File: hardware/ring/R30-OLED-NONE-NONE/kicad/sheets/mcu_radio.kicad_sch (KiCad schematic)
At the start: 0 parts

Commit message: feat(hardware): wire 30deg optical ring power and hub USB interfaces for accessibility pointing, ~$9 ring / ~$5-6 hub BOM
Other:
- note added: "MCU-side power interface scaffold: these labels match the top-sheet power contract and the firmware-facing sense/control nets."
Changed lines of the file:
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@@
   (generator_version "0.1")
   (paper "A4")
+  (text "MCU-side power interface scaffold: these labels match the top-sheet power contract and the firmware-facing sense/control nets."
+    (at 20.32 20.32 0)
+    (effects (font (size 1.27 1.27)))
+  )
+  (hierarchical_label "VREG_3V3"
+    (shape input)
+    (at 25.4 38.1 0)
+    (effects (font (size 1.27 1.27)))
+  )
+  (hierarchical_label "VBAT_SENSE"
+    (shape input)
+    (at 25.4 45.72 0)
+    (effects (font (size 1.27 1.27)))
+  )
+  (hierarchical_label "NTC_SENSE"
+    (shape input)
+    (at 25.4 53.34 0)
+    (effects (font (size 1.27 1.27)))
+  )
+  (hierarchical_label "CHARGE_EN"
+    (shape output)
+    (at 187.96 53.34 180)
+    (effects (font (size 1.27 1.27)))
+  )
   (sheet_instances
     (path "/" (page "1"))

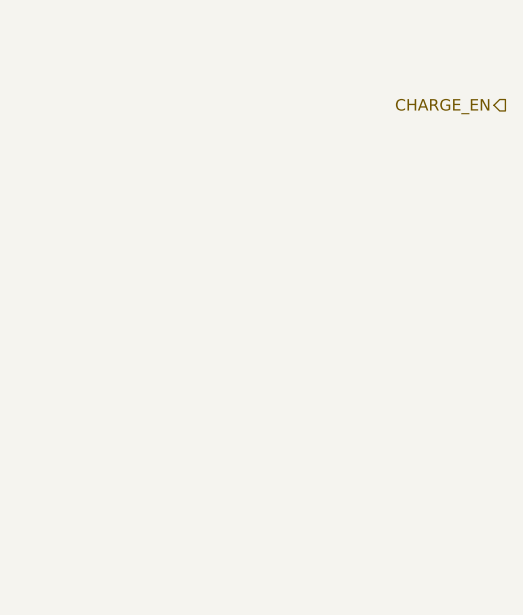
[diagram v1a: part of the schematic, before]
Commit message: feat(hardware): wire 30deg optical ring sensor/click and usb interfaces into top sheet for accessibility pointing, ~$9 ring BOM
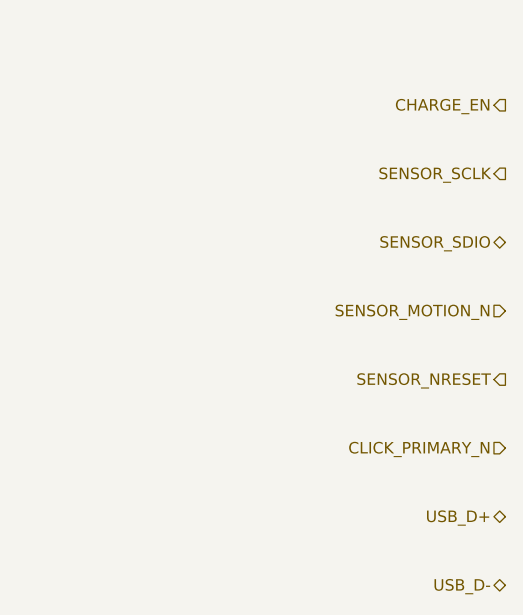
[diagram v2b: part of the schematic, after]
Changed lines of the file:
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@@
+    (effects (font (size 1.27 1.27)))
+  )
+  (hierarchical_label "SENSOR_SCLK"
+    (shape output)
+    (at 187.96 60.96 180)
+    (effects (font (size 1.27 1.27)))
+  )
+  (hierarchical_label "SENSOR_SDIO"
+    (shape bidirectional)
+    (at 187.96 68.58 180)
+    (effects (font (size 1.27 1.27)))
+  )
+  (hierarchical_label "SENSOR_MOTION_N"
+    (shape input)
+    (at 187.96 76.2 180)
+    (effects (font (size 1.27 1.27)))
+  )
+  (hierarchical_label "SENSOR_NRESET"
+    (shape output)
+    (at 187.96 83.82 180)
+    (effects (font (size 1.27 1.27)))
+  )
+  (hierarchical_label "CLICK_PRIMARY_N"
+    (shape input)
+    (at 187.96 91.44 180)
+    (effects (font (size 1.27 1.27)))
+  )
+  (hierarchical_label "USB_D+"
+    (shape bidirectional)
+    (at 187.96 99.06 180)
+    (effects (font (size 1.27 1.27)))
+  )
+  (hierarchical_label "USB_D-"
+    (shape bidirectional)
+    (at 187.96 106.68 180)
     (effects (font (size 1.27 1.27)))
   )

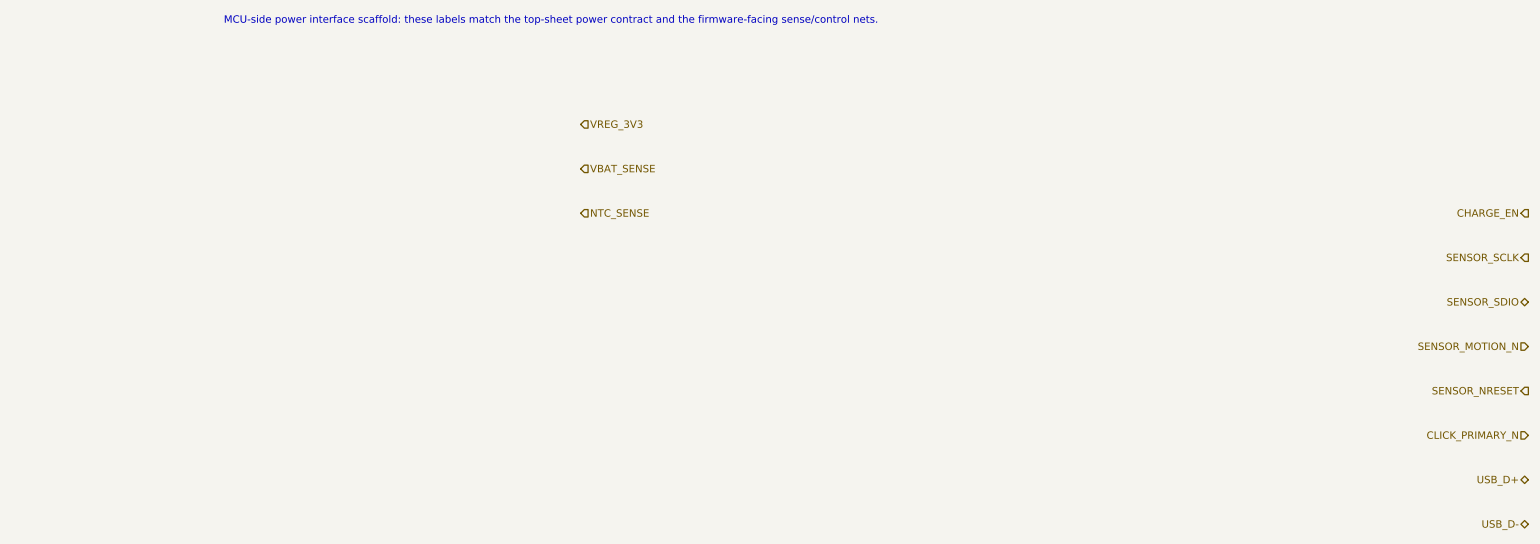
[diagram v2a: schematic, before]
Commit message: feat(hardware): lock R30 sense and schematic baseline
Design disclosure: sensing mechanism PAW3204-class optical tracking; form factor R30-OLED-NONE-NONE fingertip ring, active 30-degree ring packet; intended use BLE HID pointing for accessibility; BOM estimate ~$5.30-9.45.

Record the accepted 2N7002 charge-gate path, R7-R11 sense/status values, current KiCad red baseline, and directly linked packet truth docs.
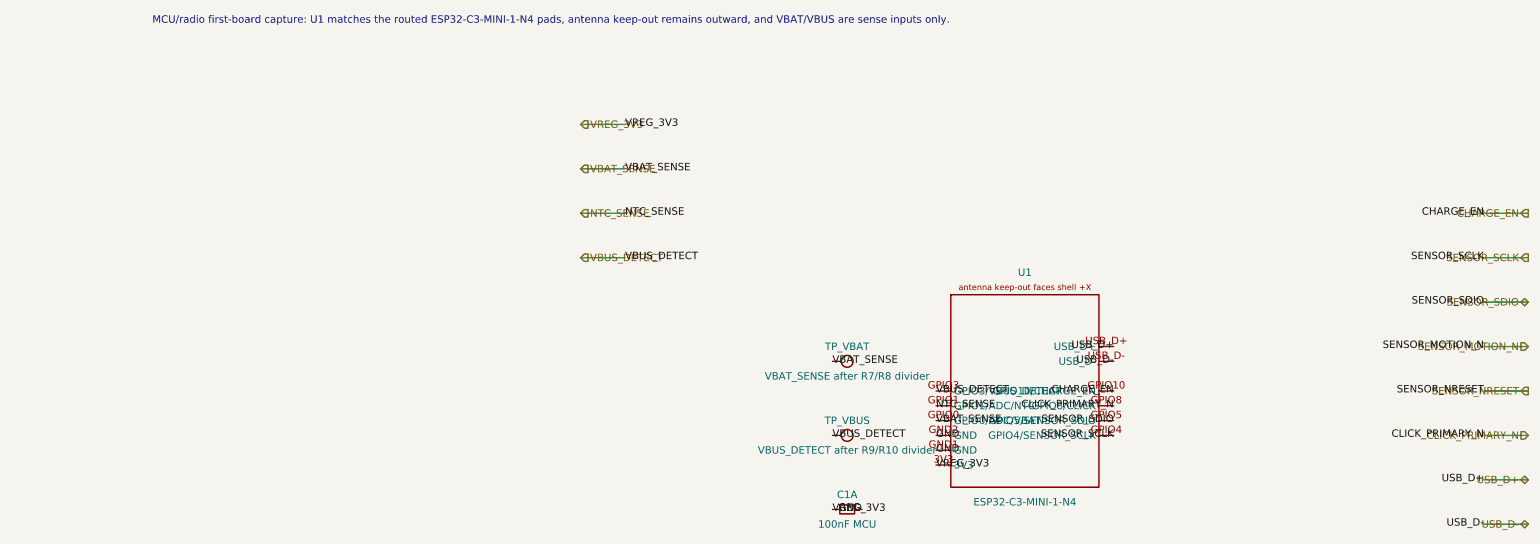
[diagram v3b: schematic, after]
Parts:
- added C1A: 100nF MCU, Capacitor_SMD:C_0402_1005Metric, symbol PowerFinger:C_0402_SUPPORT
- added TP_VBAT: VBAT_SENSE after R7/R8 divider, TestPoint:TestPoint_Pad_D1.0mm, symbol PowerFinger:TESTPAD_1MM
- added TP_VBUS: VBUS_DETECT after R9/R10 divider, TestPoint:TestPoint_Pad_D1.0mm, symbol PowerFinger:TESTPAD_1MM
- added U1: ESP32-C3-MINI-1-N4, PowerFinger_Ring:ESP32-C3-MINI-1_N4_Module_P0_AntennaRight, symbol PowerFinger:ESP32-C3-MINI-1-N4_FirstBoard
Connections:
- net CHARGE_EN: now also U1.GPIO10 (GPIO10/CHARGE_EN)
- net CLICK_PRIMARY_N: now also U1.GPIO8 (GPIO8/CLICK)
- net NTC_SENSE: now also U1.GPIO1 (GPIO1/ADC/NTC)
- net SENSOR_SCLK: now also U1.GPIO4 (GPIO4/SENSOR_SCLK)
- net SENSOR_SDIO: now also U1.GPIO5 (GPIO5/SENSOR_SDIO)
- net USB_D+: now also U1.USB_D+
- net USB_D-: now also U1.USB_D-
- net VBAT_SENSE: now also TP_VBAT.1 (TP), U1.GPIO0 (GPIO0/ADC/VBAT)
- net VREG_3V3: now also C1A.1, U1.3V3
- new net GND: C1A.2, U1.GND1 (GND), U1.GND2 (GND)
- new net VBUS_DETECT: TP_VBUS.1 (TP), U1.GPIO3 (GPIO3/VBUS_DETECT)
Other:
- note added: "MCU/radio first-board capture: U1 matches the routed ESP32-C3-MINI-1-N4 pads, antenna keep-out remains outward, and VBAT/VBUS are sense inputs only."
- note removed: "MCU-side power interface scaffold: these labels match the top-sheet power contract and the firmware-facing sense/control nets."
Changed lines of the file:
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@@
   (generator_version "0.1")
   (paper "A4")
-  (text "MCU-side power interface scaffold: these labels match the top-sheet power contract and the firmware-facing sense/control nets."
+  (text "MCU/radio first-board capture: U1 matches the routed ESP32-C3-MINI-1-N4 pads, antenna keep-out remains outward, and VBAT/VBUS are sense inputs only."
     (at 20.32 20.32 0)
     (effects (font (size 1.27 1.27)))
   )
-  (hierarchical_label "VREG_3V3"
-    (shape input)
-    (at 25.4 38.1 0)
+  (hierarchical_label "VREG_3V3" (shape input) (at 25.4 38.1 0)
     (effects (font (size 1.27 1.27)))
   )
-  (hierarchical_label "VBAT_SENSE"
-    (shape input)
-    (at 25.4 45.72 0)
+  (hierarchical_label "VBAT_SENSE" (shape input) (at 25.4 45.72 0)
     (effects (font (size 1.27 1.27)))
   )
-  (hierarchical_label "NTC_SENSE"
-    (shape input)
-    (at 25.4 53.34 0)
+  (hierarchical_label "NTC_SENSE" (shape input) (at 25.4 53.34 0)
     (effects (font (size 1.27 1.27)))
   )
-  (hierarchical_label "CHARGE_EN"
-    (shape output)
-    (at 187.96 53.34 180)
+  (hierarchical_label "VBUS_DETECT" (shape input) (at 25.4 60.96 0)
     (effects (font (size 1.27 1.27)))
   )
-  (hierarchical_label "SENSOR_SCLK"
-    (shape output)
-    (at 187.96 60.96 180)
+  (hierarchical_label "CHARGE_EN" (shape output) (at 187.96 53.34 180)
     (effects (font (size 1.27 1.27)))
   )
-  (hierarchical_label "SENSOR_SDIO"
-    (shape bidirectional)
-    (at 187.96 68.58 180)
+  (hierarchical_label "SENSOR_SCLK" (shape output) (at 187.96 60.96 180)
     (effects (font (size 1.27 1.27)))
   )
-  (hierarchical_label "SENSOR_MOTION_N"
-    (shape input)
-    (at 187.96 76.2 180)
+  (hierarchical_label "SENSOR_SDIO" (shape bidirectional) (at 187.96 68.58 180)
     (effects (font (size 1.27 1.27)))
   )
-  (hierarchical_label "SENSOR_NRESET"
-    (shape output)
-    (at 187.96 83.82 180)
+  (hierarchical_label "SENSOR_MOTION_N" (shape input) (at 187.96 76.2 180)
     (effects (font (size 1.27 1.27)))
   )
-  (hierarchical_label "CLICK_PRIMARY_N"
-    (shape input)
-    (at 187.96 91.44 180)
+  (hierarchical_label "SENSOR_NRESET" (shape output) (at 187.96 83.82 180)
     (effects (font (size 1.27 1.27)))
   )
-  (hierarchical_label "USB_D+"
-    (shape bidirectional)
-    (at 187.96 99.06 180)
+  (hierarchical_label "CLICK_PRIMARY_N" (shape input) (at 187.96 91.44 180)
     (effects (font (size 1.27 1.27)))
   )
-  (hierarchical_label "USB_D-"
-    (shape bidirectional)
-    (at 187.96 106.68 180)
+  (hierarchical_label "USB_D+" (shape bidirectional) (at 187.96 99.06 180)
     (effects (font (size 1.27 1.27)))
   )
+  (hierarchical_label "USB_D-" (shape bidirectional) (at 187.96 106.68 180)
+    (effects (font (size 1.27 1.27)))
+  )
+  (wire (pts (xy 25.4 38.1) (xy 33.02 38.1)) (stroke (width 0) (type default) (color 0 0 0 0)))
+  (wire (pts (xy 25.4 45.72) (xy 33.02 45.72)) (stroke (width 0) (type default) (color 0 0 0 0)))
+  (wire (pts (xy 25.4 53.34) (xy 33.02 53.34)) (stroke (width 0) (type default) (color 0 0 0 0)))
+  (wire (pts (xy 25.4 60.96) (xy 33.02 60.96)) (stroke (width 0) (type default) (color 0 0 0 0)))
+  (wire (pts (xy 180.34 53.34) (xy 187.96 53.34)) (stroke (width 0) (type default) (color 0 0 0 0)))
+  (wire (pts (xy 180.34 60.96) (xy 187.96 60.96)) (stroke (width 0) (type default) (color 0 0 0 0)))
+  (wire (pts (xy 180.34 68.58) (xy 187.96 68.58)) (stroke (width 0) (type default) (color 0 0 0 0)))
+  (wire (pts (xy 180.34 76.2) (xy 187.96 76.2)) (stroke (width 0) (type default) (color 0 0 0 0)))
+  (wire (pts (xy 180.34 83.82) (xy 187.96 83.82)) (stroke (width 0) (type default) (color 0 0 0 0)))
+  (wire (pts (xy 180.34 91.44) (xy 187.96 91.44)) (stroke (width 0) (type default) (color 0 0 0 0)))
+  (wire (pts (xy 180.34 99.06) (xy 187.96 99.06)) (stroke (width 0) (type default) (color 0 0 0 0)))
+  (wire (pts (xy 180.34 106.68) (xy 187.96 106.68)) (stroke (width 0) (type default) (color 0 0 0 0)))
+  (label "VREG_3V3" (at 33.02 38.1 0) (effects (font (size 1.27 1.27))))
+  (label "VBAT_SENSE" (at 33.02 45.72 0) (effects (font (size 1.27 1.27))))
+  (label "NTC_SENSE" (at 33.02 53.34 0) (effects (font (size 1.27 1.27))))
+  (label "VBUS_DETECT" (at 33.02 60.96 0) (effects (font (size 1.27 1.27))))
+  (label "CHARGE_EN" (at 180.34 53.34 180) (effects (font (size 1.27 1.27))))
+  (label "SENSOR_SCLK" (at 180.34 60.96 180) (effects (font (size 1.27 1.27))))
+  (label "SENSOR_SDIO" (at 180.34 68.58 180) (effects (font (size 1.27 1.27))))
+  (label "SENSOR_MOTION_N" (at 180.34 76.2 180) (effects (font (size 1.27 1.27))))
+  (label "SENSOR_NRESET" (at 180.34 83.82 180) (effects (font (size 1.27 1.27))))
+  (label "CLICK_PRIMARY_N" (at 180.34 91.44 180) (effects (font (size 1.27 1.27))))
+  (label "USB_D+" (at 180.34 99.06 180) (effects (font (size 1.27 1.27))))
+  (label "USB_D-" (at 180.34 106.68 180) (effects (font (size 1.27 1.27))))
+  (symbol (lib_id "PowerFinger:ESP32-C3-MINI-1-N4_FirstBoard") (at 101.6 83.82 0) (unit 1)
+    (in_bom yes) (on_board yes) (dnp no)
+    (property "Reference" "U1" (at 101.6 63.5 0)
+      (effects (font (size 1.27 1.27)))
+    )
+    (property "Value" "ESP32-C3-MINI-1-N4" (at 101.6 102.87 0)
+      (effects (font (size 1.27 1.27)))
+    )
+    (property "Footprint" "PowerFinger_Ring:ESP32-C3-MINI-1_N4_Module_P0_AntennaRight" (at 101.6 105.41 0)
+      (effects (font (size 1.27 1.27)) hide)
+    )
+    (property "Datasheet" "https://www.espressif.com/sites/default/files/documentation/esp32-c3-mini-1_datasheet_en.pdf" (at 101.6 107.95 0)
+      (effects (font (size 1.27 1.27)) hide)
+    )
+    (pin "3V3")
+    (pin "GND1")
+    (pin "GPIO0")
+    (pin "GPIO1")
+    (pin "GPIO3")
+    (pin "GPIO4")
+    (pin "GPIO5")
+    (pin "GPIO8")
+    (pin "GPIO10")
+    (pin "USB_D-")
+    (pin "USB_D+")
+    (pin "GND2")
+    (instances
+      (project "r30_oled_none_none"
+        (path "/" (reference "U1") (unit 1))
+      )
+    )
+  )
+  (symbol (lib_id "PowerFinger:C_0402_SUPPORT") (at 71.12 104.14 0) (unit 1)
+    (in_bom yes) (on_board yes) (dnp no)
+    (property "Reference" "C1A" (at 71.12 101.6 0)
+      (effects (font (size 1.27 1.27)))
+    )
+    (property "Value" "100nF MCU" (at 71.12 106.68 0)
+      (effects (font (size 1.27 1.27)))
+    )
+    (property "Footprint" "Capacitor_SMD:C_0402_1005Metric" (at 71.12 109.22 0)
+      (effects (font (size 1.27 1.27)) hide)
+    )
+    (property "Datasheet" "" (at 71.12 111.76 0)
+      (effects (font (size 1.27 1.27)) hide)
+    )
+    (pin "1")
+    (pin "2")
+    (instances
+      (project "r30_oled_none_none"
+        (path "/" (reference "C1A") (unit 1))
+      )
+    )
+  )
+  (symbol (lib_id "PowerFinger:TESTPAD_1MM") (at 71.12 78.74 0) (unit 1)
+    (in_bom yes) (on_board yes) (dnp no)
+    (property "Reference" "TP_VBAT" (at 71.12 76.2 0)
+      (effects (font (size 1.27 1.27)))
+    )
+    (property "Value" "VBAT_SENSE after R7/R8 divider" (at 71.12 81.28 0)
+      (effects (font (size 1.27 1.27)))
+    )
+    (property "Footprint" "TestPoint:TestPoint_Pad_D1.0mm" (at 71.12 83.82 0)
+      (effects (font (size 1.27 1.27)) hide)
+    )
+    (pin "1")
+    (instances
+      (project "r30_oled_none_none"
+        (path "/" (reference "TP_VBAT") (unit 1))
+      )
+    )
+  )
+  (symbol (lib_id "PowerFinger:TESTPAD_1MM") (at 71.12 91.44 0) (unit 1)
+    (in_bom yes) (on_board yes) (dnp no)
+    (property "Reference" "TP_VBUS" (at 71.12 88.9 0)
+      (effects (font (size 1.27 1.27)))
+    )
+    (property "Value" "VBUS_DETECT after R9/R10 divider" (at 71.12 93.98 0)
+      (effects (font (size 1.27 1.27)))
+    )
+    (property "Footprint" "TestPoint:TestPoint_Pad_D1.0mm" (at 71.12 96.52 0)
+      (effects (font (size 1.27 1.27)) hide)
+    )
+    (pin "1")
+    (instances
+      (project "r30_oled_none_none"
+        (path "/" (reference "TP_VBUS") (unit 1))
+      )
+    )
+  )
+  (label "VREG_3V3" (at 86.36 96.52 0) (effects (font (size 1.27 1.27))))
+  (label "GND" (at 86.36 93.98 0) (effects (font (size 1.27 1.27))))
+  (label "GND" (at 86.36 91.44 0) (effects (font (size 1.27 1.27))))
+  (label "VBAT_SENSE" (at 86.36 88.9 0) (effects (font (size 1.27 1.27))))
+  (label "NTC_SENSE" (at 86.36 86.36 0) (effects (font (size 1.27 1.27))))
+  (label "VBUS_DETECT" (at 86.36 83.82 0) (effects (font (size 1.27 1.27))))
+  (label "SENSOR_SCLK" (at 116.84 91.44 180) (effects (font (size 1.27 1.27))))
+  (label "SENSOR_SDIO" (at 116.84 88.9 180) (effects (font (size 1.27 1.27))))
+  (label "CLICK_PRIMARY_N" (at 116.84 86.36 180) (effects (font (size 1.27 1.27))))
+  (label "CHARGE_EN" (at 116.84 83.82 180) (effects (font (size 1.27 1.27))))
+  (label "USB_D-" (at 116.84 78.74 180) (effects (font (size 1.27 1.27))))
+  (label "USB_D+" (at 116.84 76.2 180) (effects (font (size 1.27 1.27))))
+  (label "VREG_3V3" (at 68.58 104.14 0) (effects (font (size 1.27 1.27))))
+  (label "GND" (at 73.66 104.14 180) (effects (font (size 1.27 1.27))))
+  (label "VBAT_SENSE" (at 68.58 78.74 0) (effects (font (size 1.27 1.27))))
+  (label "VBUS_DETECT" (at 68.58 91.44 0) (effects (font (size 1.27 1.27))))
   (sheet_instances
     (path "/" (page "1"))

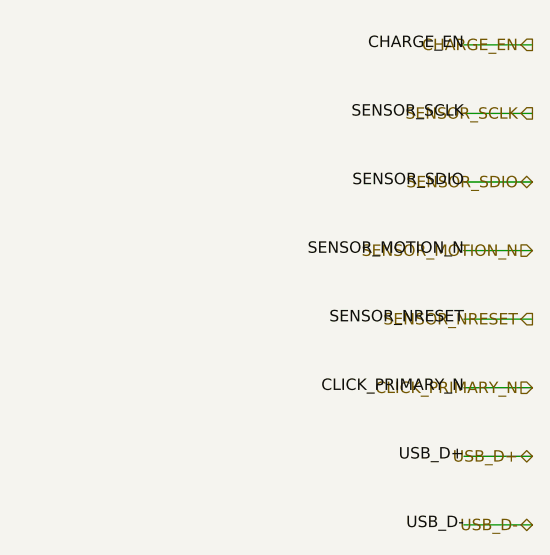
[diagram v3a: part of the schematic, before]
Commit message: fix(r30): clean schematic erc library baseline
Design disclosure: sensing mechanism PAW3204-class optical tracking; form factor R30-OLED-NONE-NONE fingertip ring, active 30-degree ring packet; intended use BLE HID pointing for accessibility; BOM estimate ~$5.30-9.45.

Materialize the project-local PowerFinger symbol and PowerFinger_Ring footprint libraries, wire sheet-interface labels, keep PAW3204 reset/motion local to sensor test pads, and update the verified KiCad snapshot to ERC=0, DRC=349, unconnected=41, parity=118.
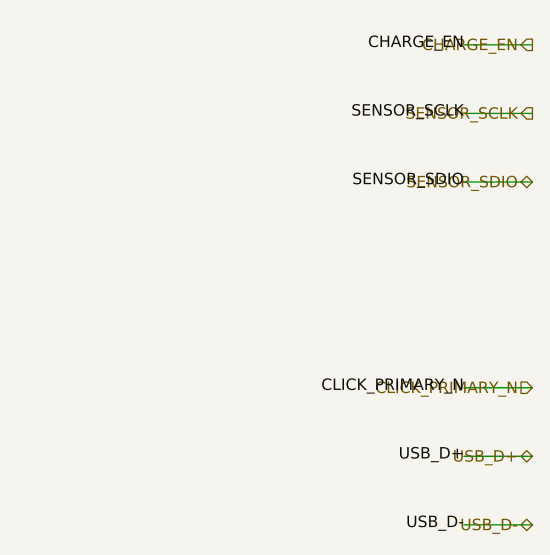
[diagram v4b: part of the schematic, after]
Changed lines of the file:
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@@
     (effects (font (size 1.27 1.27)))
   )
-  (hierarchical_label "SENSOR_MOTION_N" (shape input) (at 187.96 76.2 180)
-    (effects (font (size 1.27 1.27)))
-  )
-  (hierarchical_label "SENSOR_NRESET" (shape output) (at 187.96 83.82 180)
-    (effects (font (size 1.27 1.27)))
-  )
-  (hierarchical_label "CLICK_PRIMARY_N" (shape input) (at 187.96 91.44 180)
+      (hierarchical_label "CLICK_PRIMARY_N" (shape input) (at 187.96 91.44 180)
     (effects (font (size 1.27 1.27)))
   )
@@
   (wire (pts (xy 180.34 60.96) (xy 187.96 60.96)) (stroke (width 0) (type default) (color 0 0 0 0)))
   (wire (pts (xy 180.34 68.58) (xy 187.96 68.58)) (stroke (width 0) (type default) (color 0 0 0 0)))
-  (wire (pts (xy 180.34 76.2) (xy 187.96 76.2)) (stroke (width 0) (type default) (color 0 0 0 0)))
-  (wire (pts (xy 180.34 83.82) (xy 187.96 83.82)) (stroke (width 0) (type default) (color 0 0 0 0)))
-  (wire (pts (xy 180.34 91.44) (xy 187.96 91.44)) (stroke (width 0) (type default) (color 0 0 0 0)))
+      (wire (pts (xy 180.34 91.44) (xy 187.96 91.44)) (stroke (width 0) (type default) (color 0 0 0 0)))
   (wire (pts (xy 180.34 99.06) (xy 187.96 99.06)) (stroke (width 0) (type default) (color 0 0 0 0)))
   (wire (pts (xy 180.34 106.68) (xy 187.96 106.68)) (stroke (width 0) (type default) (color 0 0 0 0)))
@@
   (label "SENSOR_SCLK" (at 180.34 60.96 180) (effects (font (size 1.27 1.27))))
   (label "SENSOR_SDIO" (at 180.34 68.58 180) (effects (font (size 1.27 1.27))))
-  (label "SENSOR_MOTION_N" (at 180.34 76.2 180) (effects (font (size 1.27 1.27))))
-  (label "SENSOR_NRESET" (at 180.34 83.82 180) (effects (font (size 1.27 1.27))))
-  (label "CLICK_PRIMARY_N" (at 180.34 91.44 180) (effects (font (size 1.27 1.27))))
+      (label "CLICK_PRIMARY_N" (at 180.34 91.44 180) (effects (font (size 1.27 1.27))))
   (label "USB_D+" (at 180.34 99.06 180) (effects (font (size 1.27 1.27))))
   (label "USB_D-" (at 180.34 106.68 180) (effects (font (size 1.27 1.27))))
